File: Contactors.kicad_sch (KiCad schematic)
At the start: 8 parts, among them U1 EL3H7, U6 EL3H7

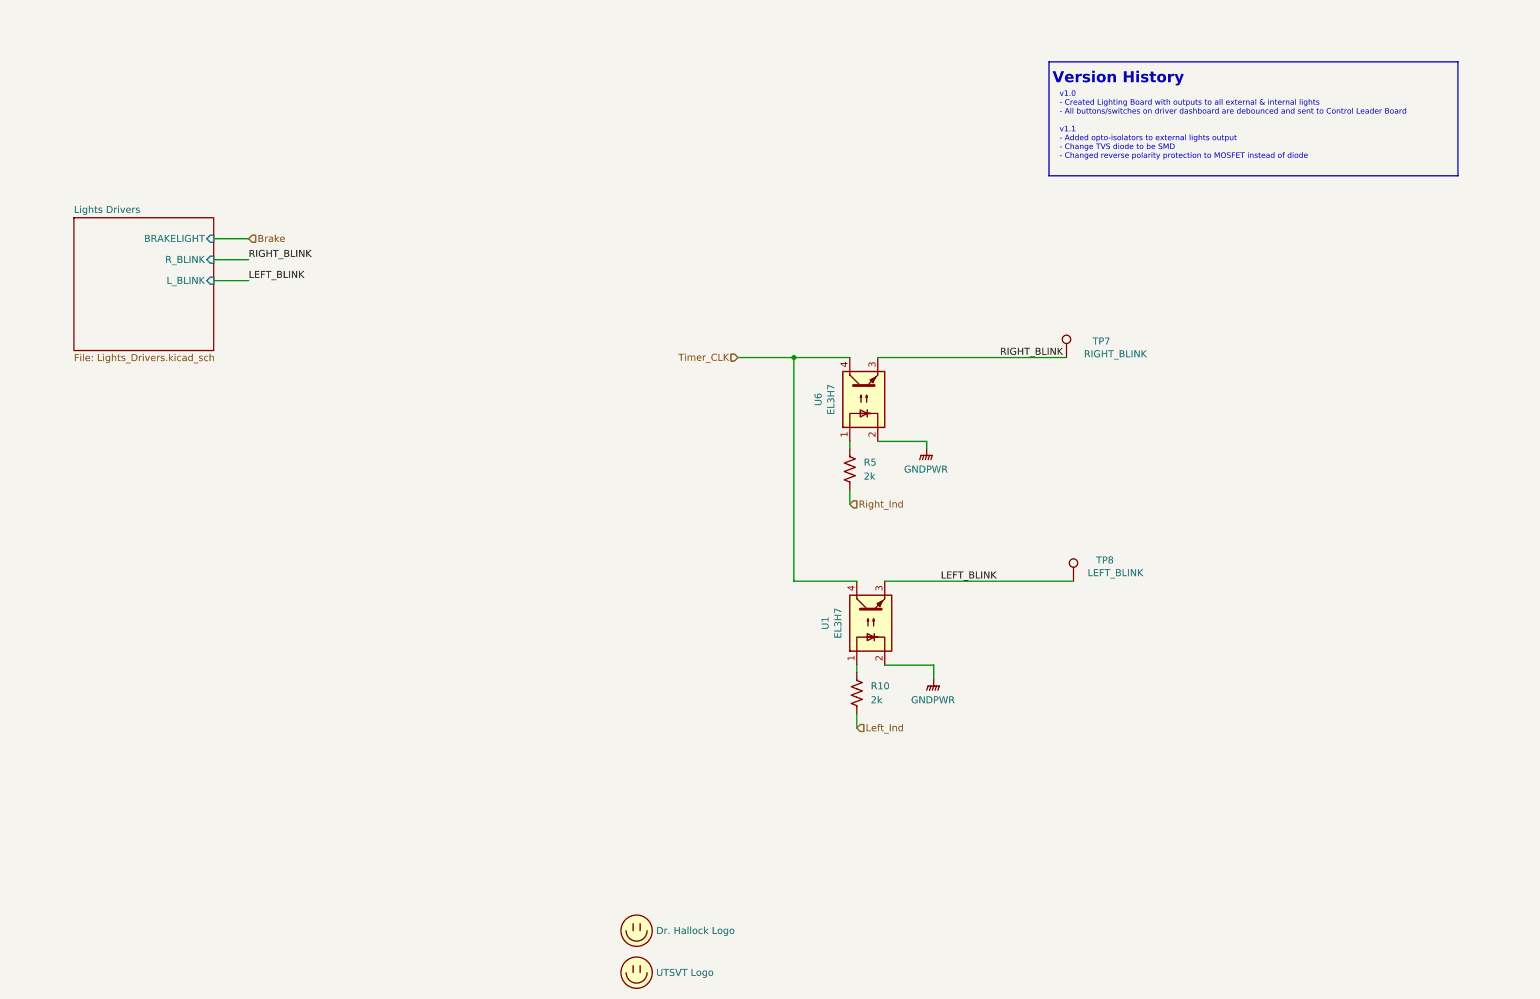
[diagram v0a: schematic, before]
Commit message: renamed power state indicators to contactors and removed unused contactors, added current limiting resistors to lights drivers, changed mosfet to new mosfet
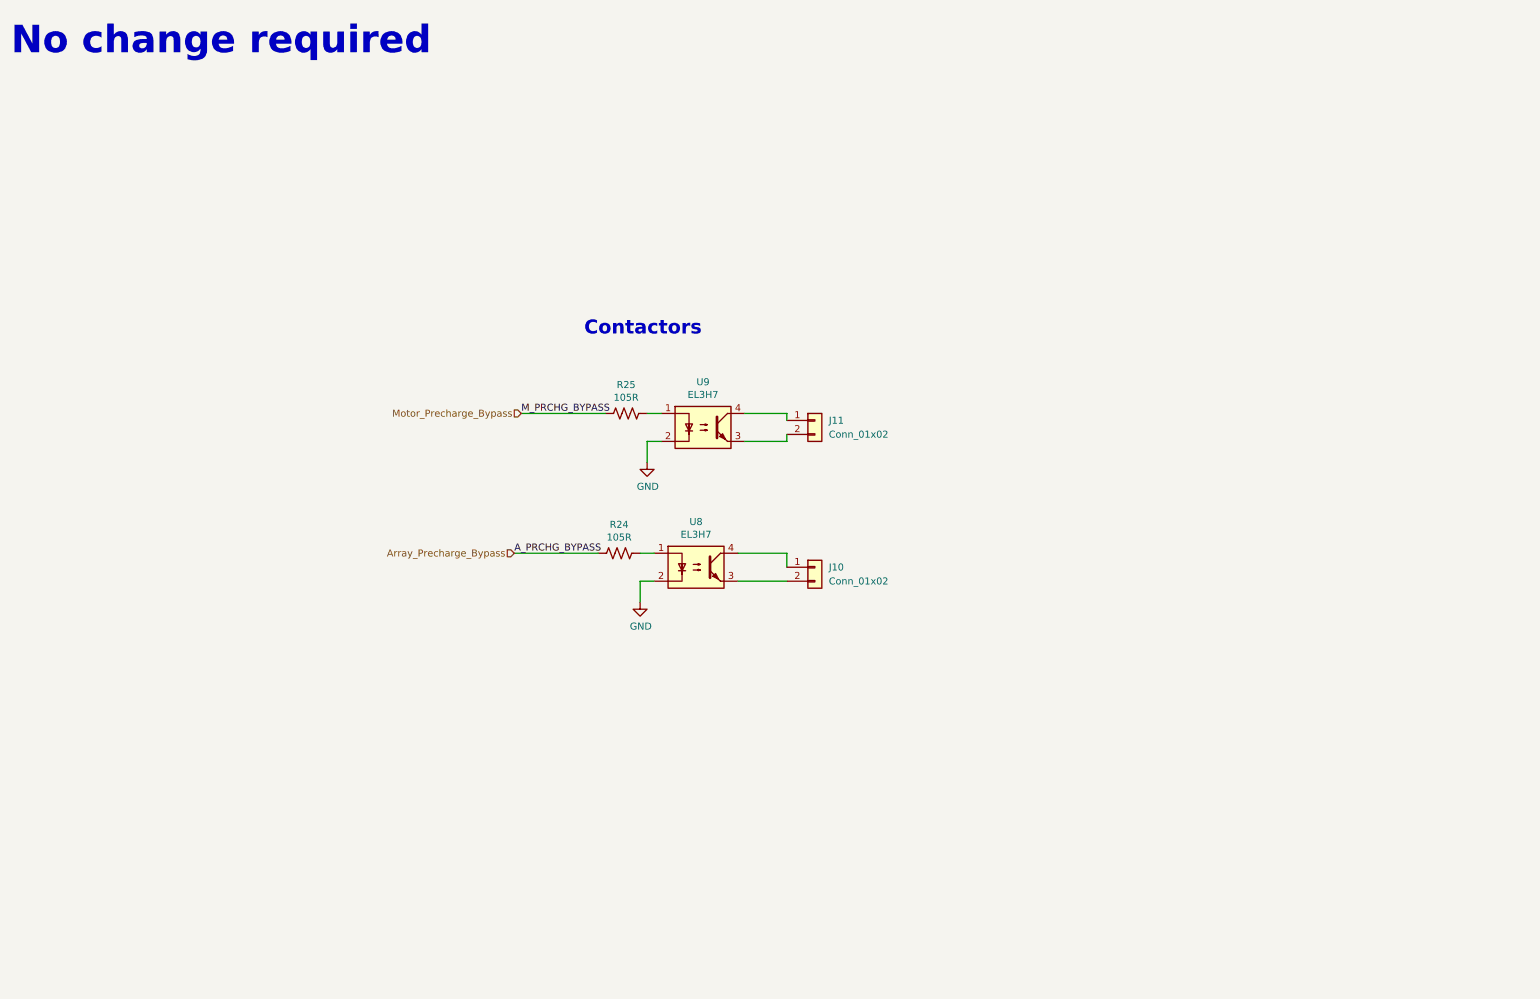
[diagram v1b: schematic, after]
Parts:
- removed LOGO3: Dr. Hallock Logo, UTSVT_Special:Hallock_Image_Small, symbol Controls-LightingPCB-rescue:Logo_Placeholder-utsvt-misc
- removed LOGO4: UTSVT Logo, UTSVT_Special:UTSVT_Logo_Symbol, symbol Controls-LightingPCB-rescue:Logo_Placeholder-utsvt-misc
- removed R10, R5: 2k, Resistor_SMD:R_0805_2012Metric, symbol Device:R_US
- removed TP7: RIGHT_BLINK, TestPoint:TestPoint_Pad_1.5x1.5mm, symbol Connector:TestPoint
- removed TP8: LEFT_BLINK, TestPoint:TestPoint_Pad_1.5x1.5mm, symbol Connector:TestPoint
- removed U1, U6: EL3H7, Package_DIP:DIP-4_W7.62mm, symbol Isolator:SFH617A-1
- added J10, J11: Conn_01x02, Connector_Molex:Molex_Micro-Fit_3.0_43650-0215_1x02_P3.00mm_Vertical, symbol Connector_Generic:Conn_01x02
- added R24, R25: 105R, Resistor_SMD:R_0805_2012Metric, symbol Device:R_US
- added U8, U9: EL3H7, Package_DIP:DIP-4_W7.62mm, symbol Isolator:SFH617A-1
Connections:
- new net: R24.1, U8.1
- new net: J10.2 (Pin_2), U8.3
- new net: J10.1 (Pin_1), U8.4
- new net: R25.1, U9.1
- new net: J11.2 (Pin_2), U9.3
- new net: J11.1 (Pin_1), U9.4
- new net Array_Precharge_Bypass: R24.2
- new net GND: U8.2, U9.2
- new net Motor_Precharge_Bypass: R25.2
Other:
- removed sheet Lights Drivers
- note added: "Contactors"
- note added: "No change required"
- note removed: "Version History"
- note removed: "v1.0 - Created Lighting Board with outputs to all external & internal lights - All buttons/switches on driver dashboard are debounced and sent to Control Leader Board v1.1 - Added opto-isolators to external lights output - Change TVS diode to be SMD - Changed reverse polarity protection to MOSFET instead of diode"

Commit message: Added/checked datasheet links/part numbers, deleted accel_pot2 and brake_pot2 hierarchical labels and changed corresponding pins (PC2, PC3) to GPIO on the now-2x5 extra GPIO connector.
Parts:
- J10, J11: P/N (none) -> 43650-0215
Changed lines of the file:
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@@
 			)
 		)
-		(property "Datasheet" "https://everlightamericas.com/index.php?controller=attachment&id_attachment=2584"
+		(property "Datasheet" "https://www.mouser.com/ProductDetail/Everlight/EL3H7DTA-VG?qs=8PzhAHr7IdO5ivSzPAFioA%3D%3D&utm_id=21629221803&gad_source=1&gclid=Cj0KCQiArby5BhCDARIsAIJvjIRxO0jcjcKfnV1hER0ZGDMF9W_FecGmdKXwVqQCsmJYIZvEtRfuUkAaAnFwEALw_wcB"
 			(at 139.7 115.57 0)
 			(effects
@@
 			)
 		)
-		(property "Datasheet" "~"
+		(property "Datasheet" "https://www.mouser.com/ProductDetail/Vishay-Dale/CRCW0805105RFKEA?qs=sGAEpiMZZMvdGkrng054txEw7b1YnvGufwlC1LWQIEg%3D"
 			(at 125.73 113.03 0)
 			(effects
@@
 			)
 		)
-		(property "Datasheet" "https://everlightamericas.com/index.php?controller=attachment&id_attachment=2584"
+		(property "Datasheet" "https://www.mouser.com/ProductDetail/Everlight/EL3H7DTA-VG?qs=8PzhAHr7IdO5ivSzPAFioA%3D%3D&utm_id=21629221803&gad_source=1&gclid=Cj0KCQiArby5BhCDARIsAIJvjIRxO0jcjcKfnV1hER0ZGDMF9W_FecGmdKXwVqQCsmJYIZvEtRfuUkAaAnFwEALw_wcB"
 			(at 140.97 90.17 0)
 			(effects
@@
 			)
 		)
-		(property "Datasheet" "~"
+		(property "Datasheet" "https://www.mouser.com/ProductDetail/Vishay-Dale/CRCW0805105RFKEA?qs=sGAEpiMZZMvdGkrng054txEw7b1YnvGufwlC1LWQIEg%3D"
 			(at 127 87.63 0)
 			(effects
@@
 			)
 		)
+		(property "P/N" "43650-0215"
+			(at 161.29 88.9 0)
+			(effects
+				(font
+					(size 1.27 1.27)
+				)
+				(hide yes)
+			)
+		)
 		(pin "1"
 		)
@@
 			(at 161.29 115.57 0)
 			(effects
+				(font
+					(size 1.27 1.27)
+				)
+				(hide yes)
+			)
+		)
+		(property "P/N" "43650-0215"
+			(at 161.29 115.57 0)
+			(effects

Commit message: Changed EL3H7 footprint from through-hole to SMD.
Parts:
- U8, U9: footprint Package_DIP:DIP-4_W7.62mm -> Package_SO:SSOP-4_4.4x2.6mm_P1.27mm
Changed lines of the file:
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@@
 			)
 		)
-		(property "Footprint" "Package_DIP:DIP-4_W7.62mm"
+		(property "Footprint" "Package_SO:SSOP-4_4.4x2.6mm_P1.27mm"
 			(at 134.62 120.65 0)
 			(effects
@@
 			)
 		)
-		(property "Footprint" "Package_DIP:DIP-4_W7.62mm"
+		(property "Footprint" "Package_SO:SSOP-4_4.4x2.6mm_P1.27mm"
 			(at 135.89 95.25 0)
 			(effects

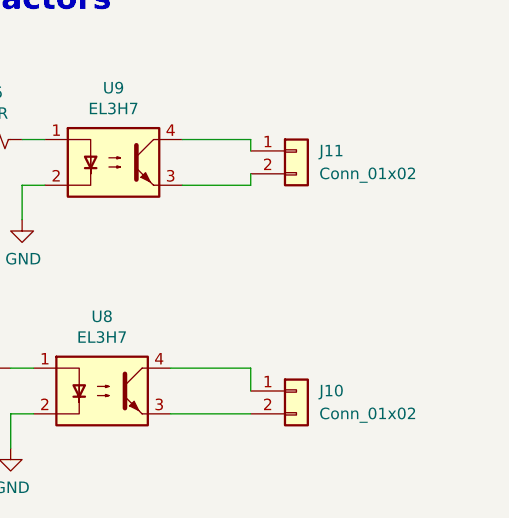
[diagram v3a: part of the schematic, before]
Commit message: Moved some things inward and squished board, added some labels, broke some traces up (sorry Krish 😣)
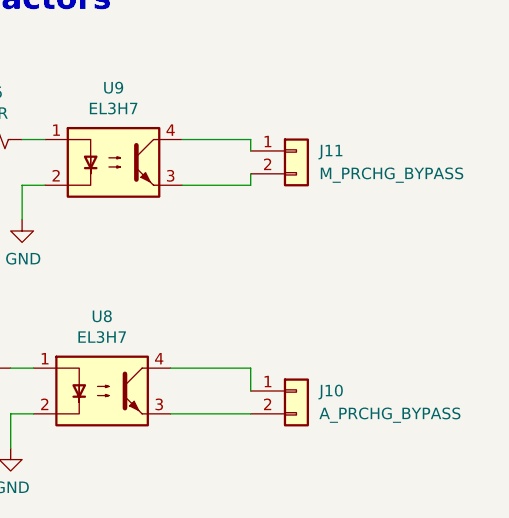
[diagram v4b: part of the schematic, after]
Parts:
- J10: value Conn_01x02 -> A_PRCHG_BYPASS
- J11: value Conn_01x02 -> M_PRCHG_BYPASS
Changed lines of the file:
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@@
 			)
 		)
-		(property "Value" "Conn_01x02"
+		(property "Value" "M_PRCHG_BYPASS"
 			(at 163.83 91.4399 0)
 			(effects
@@
 			)
 		)
-		(property "Value" "Conn_01x02"
+		(property "Value" "A_PRCHG_BYPASS"
 			(at 163.83 118.1099 0)
 			(effects

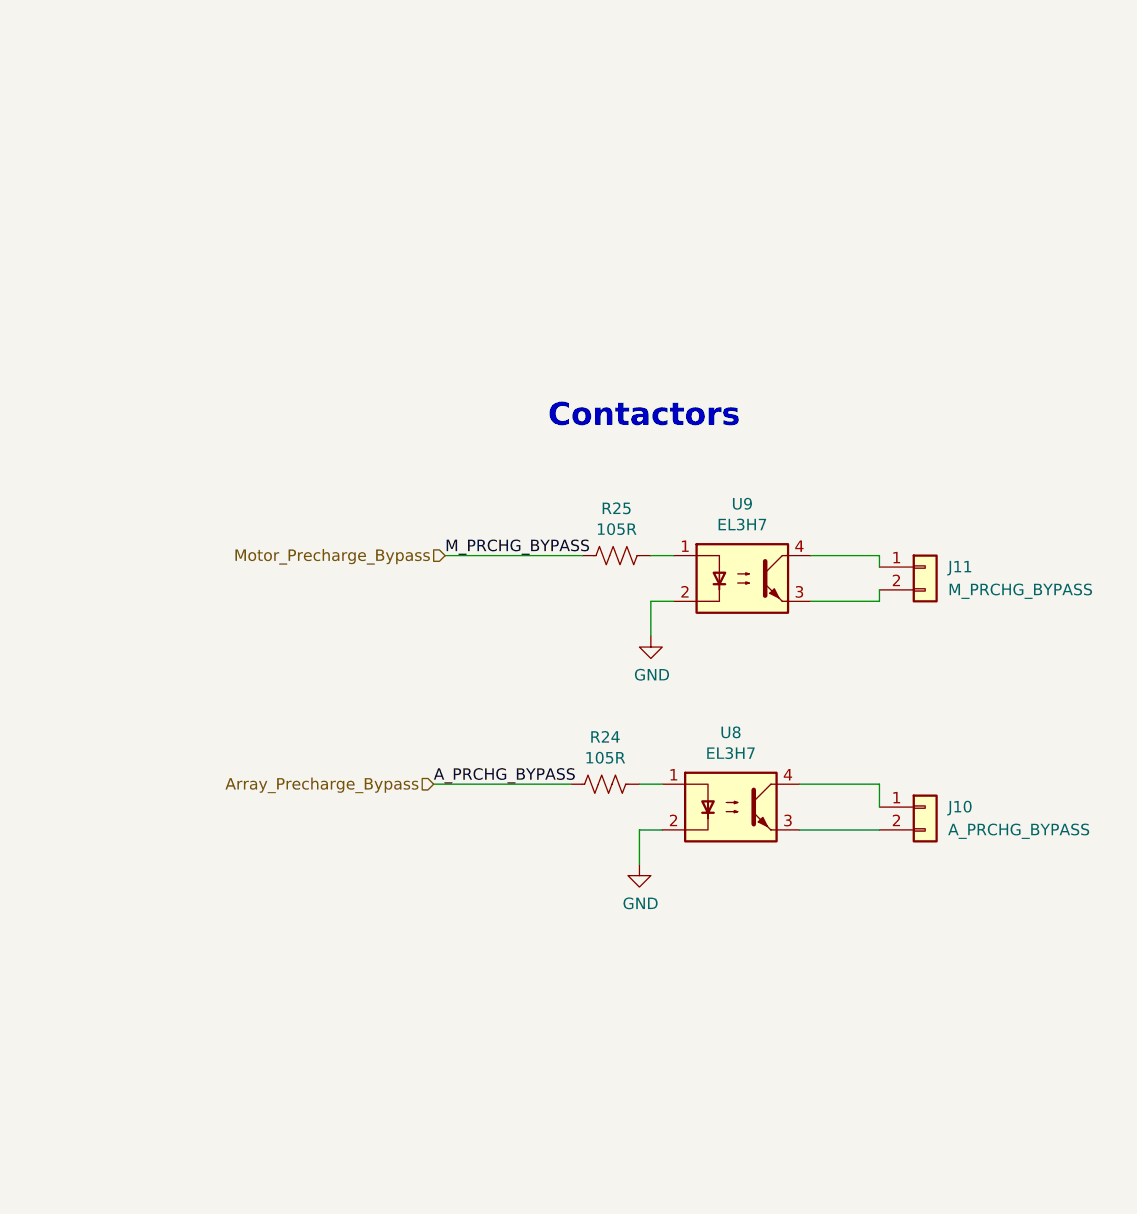
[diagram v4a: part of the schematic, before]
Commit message: Added motor contactor, contactor sense pins, deleted extra GPIO connector 2 since we are now using more of the extra GPIO pins; added new components to layout.
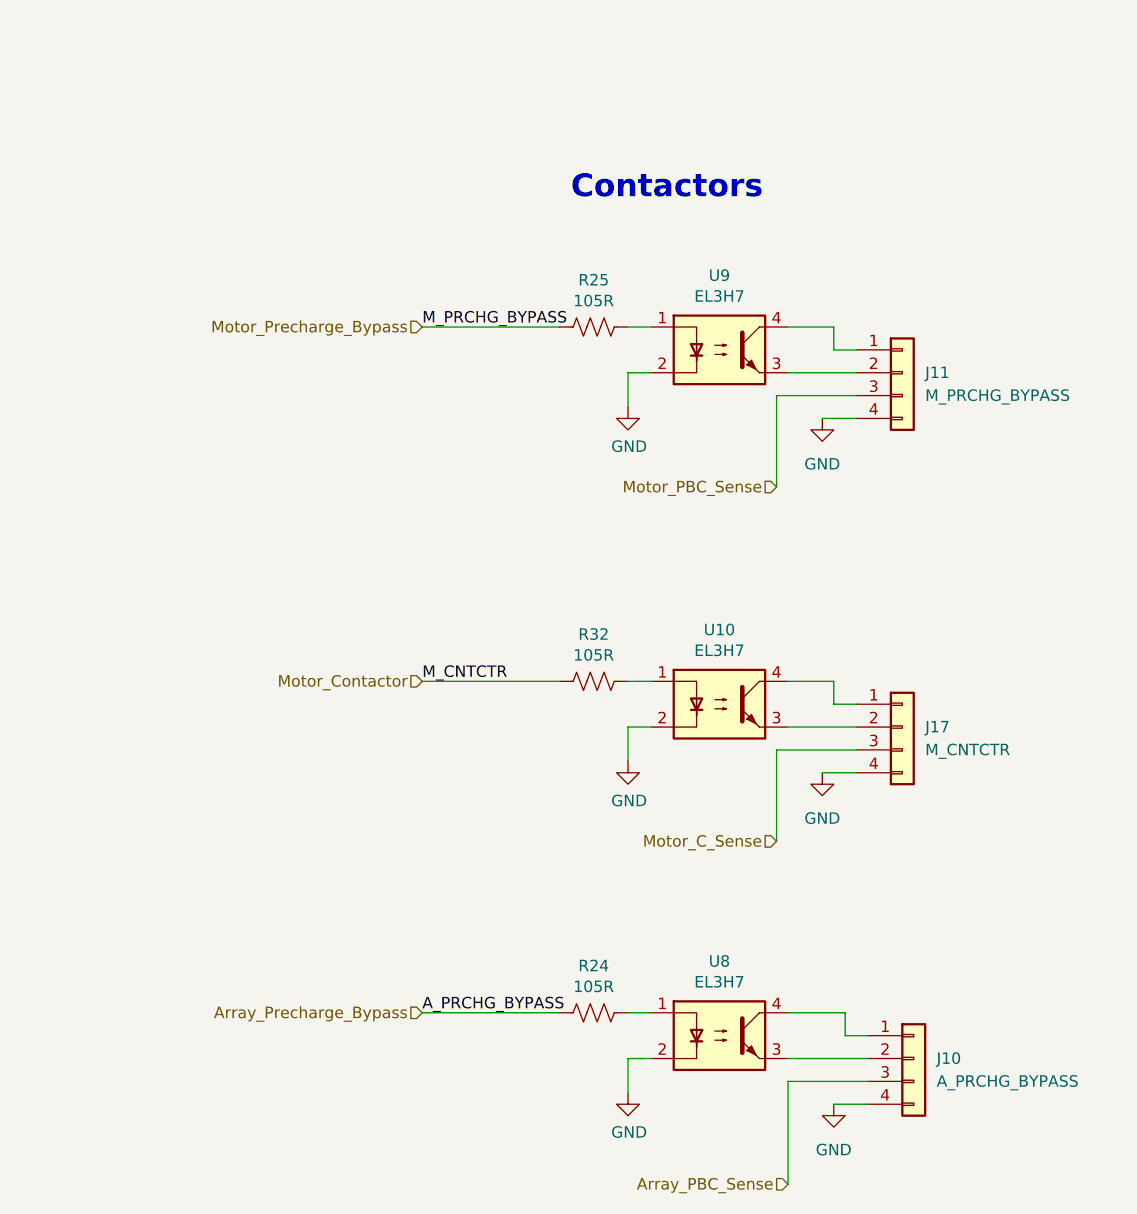
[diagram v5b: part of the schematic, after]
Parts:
- added J17: M_CNTCTR, Connector_Molex:Molex_Micro-Fit_3.0_43650-0415_1x04_P3.00mm_Vertical, symbol Connector_Generic:Conn_01x04
- added R32: 105R, Resistor_SMD:R_0805_2012Metric, symbol Device:R_US
- added U10: EL3H7, Package_SO:SSOP-4_4.4x2.6mm_P1.27mm, symbol Isolator:SFH617A-1
- J10, J11: footprint Connector_Molex:Molex_Micro-Fit_3.0_43650-0215_1x02_P3.00mm_Vertical -> Connector_Molex:Molex_Micro-Fit_3.0_43650-0415_1x04_P3.00mm_Vertical; symbol Connector_Generic:Conn_01x02 -> Connector_Generic:Conn_01x04
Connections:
- net GND: now also J10.4 (Pin_4), J11.4 (Pin_4), J17.4 (Pin_4), U10.2
- new net: R32.1, U10.1
- new net: J17.1 (Pin_1), U10.4
- new net: J17.2 (Pin_2), U10.3
- new net Array_PBC_Sense: J10.3 (Pin_3)
- new net Motor_C_Sense: J17.3 (Pin_3)
- new net Motor_Contactor: R32.2
- new net Motor_PBC_Sense: J11.3 (Pin_3)
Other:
- moved on the sheet: R24, R25, U8, U9

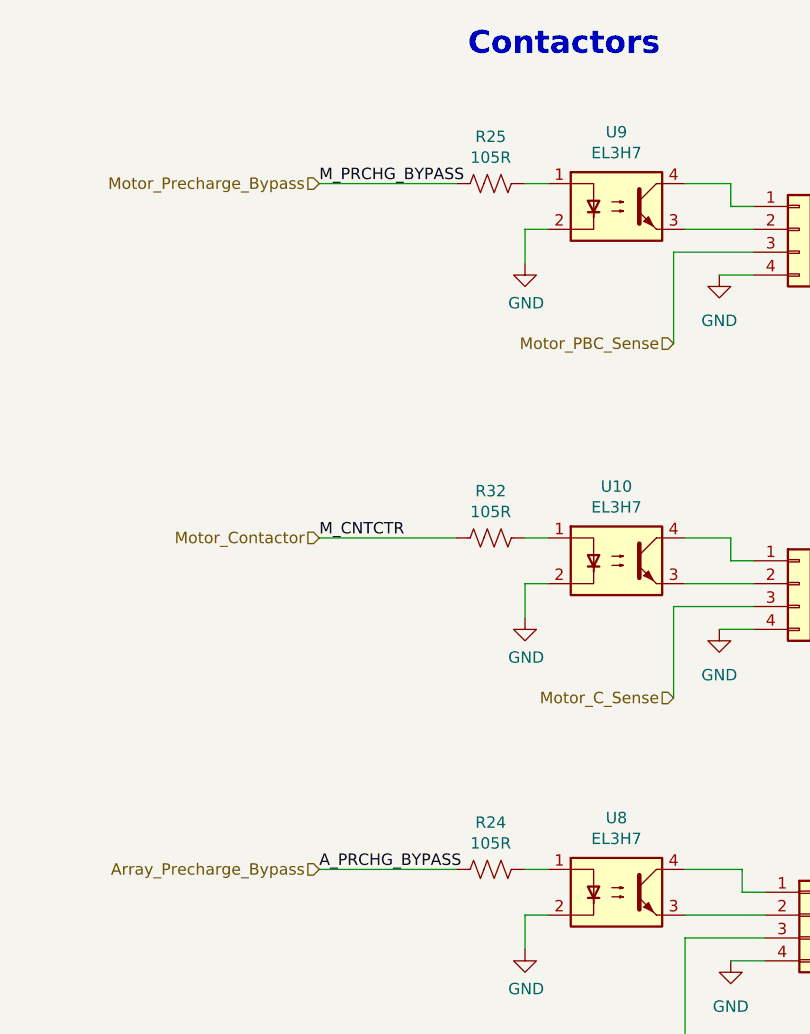
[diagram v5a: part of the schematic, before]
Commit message: Updated some symbols to use common libraries (and get rid of warnings.
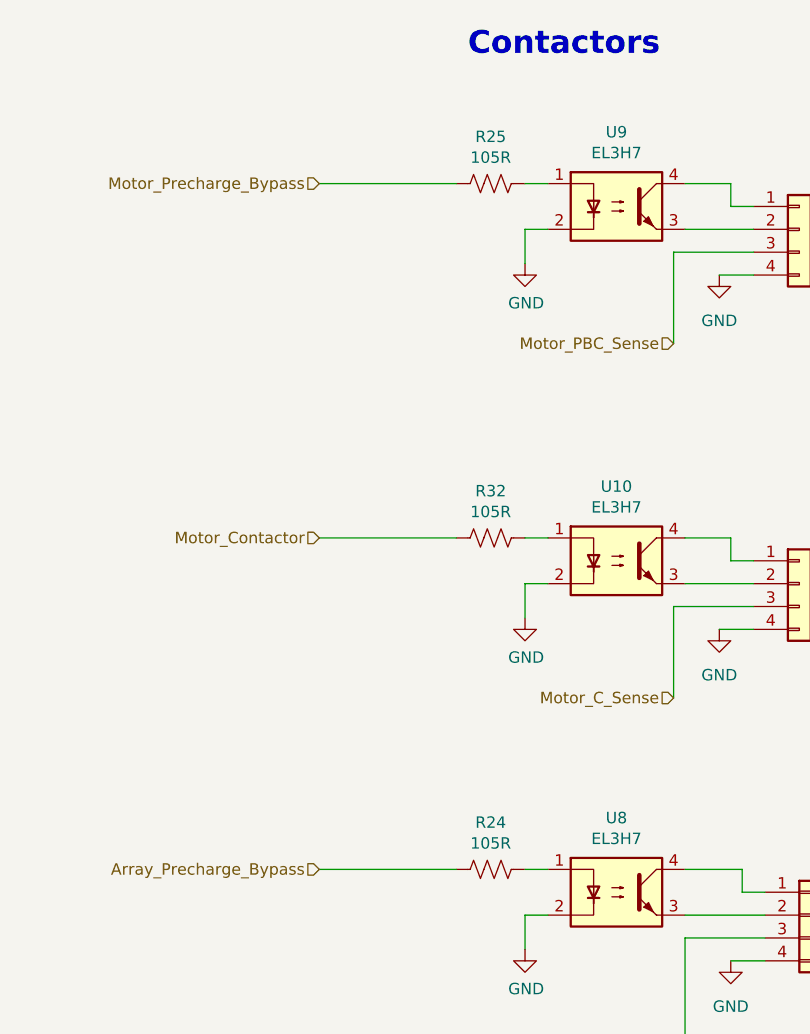
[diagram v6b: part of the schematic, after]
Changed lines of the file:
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@@
-		)
-	)
-	(label "A_PRCHG_BYPASS"
-		(at 105.41 138.43 0)
-		(fields_autoplaced yes)
-		(effects
-			(font
-				(size 1.27 1.27)
-			)
-			(justify left bottom)
-		)
-	)
-	(label "M_PRCHG_BYPASS"
-		(at 105.41 62.23 0)
-		(fields_autoplaced yes)
-		(effects
-			(font
-				(size 1.27 1.27)
-			)
-			(justify left bottom)
-		)
-	)
-	(label "M_CNTCTR"
-		(at 105.41 101.6 0)
-		(fields_autoplaced yes)
-		(effects
-			(font
-				(size 1.27 1.27)
-			)
-			(justify left bottom)
 		)
 	)
